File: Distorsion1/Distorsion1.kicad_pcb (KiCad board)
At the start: 2 copper layers, 35 x 79.4 mm, 39 parts, among them J1 Jack-DC, J2 IN, J3 OUT, Sw1 Footswitch, U1 TL082

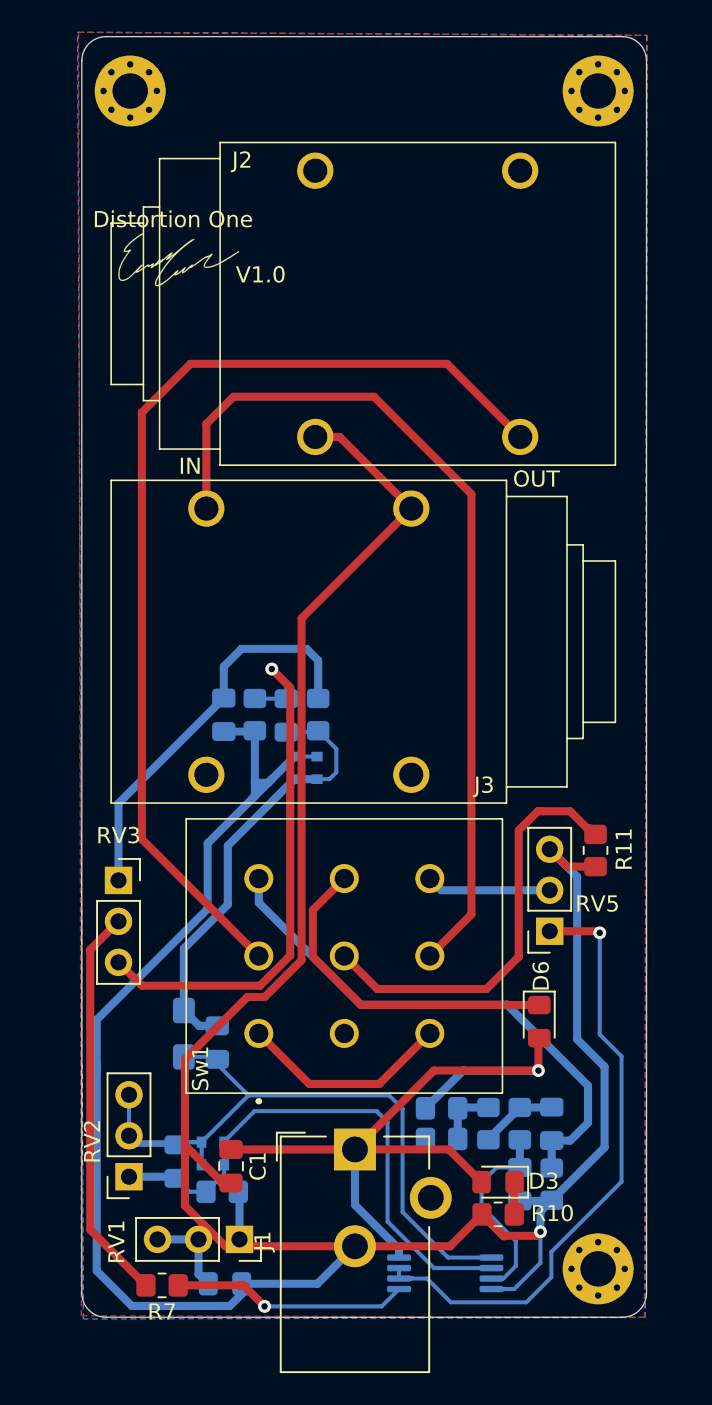
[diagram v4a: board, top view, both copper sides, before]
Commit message: PCB2.0(cambio de parte mecanica y circuito mas cerca de la señal)
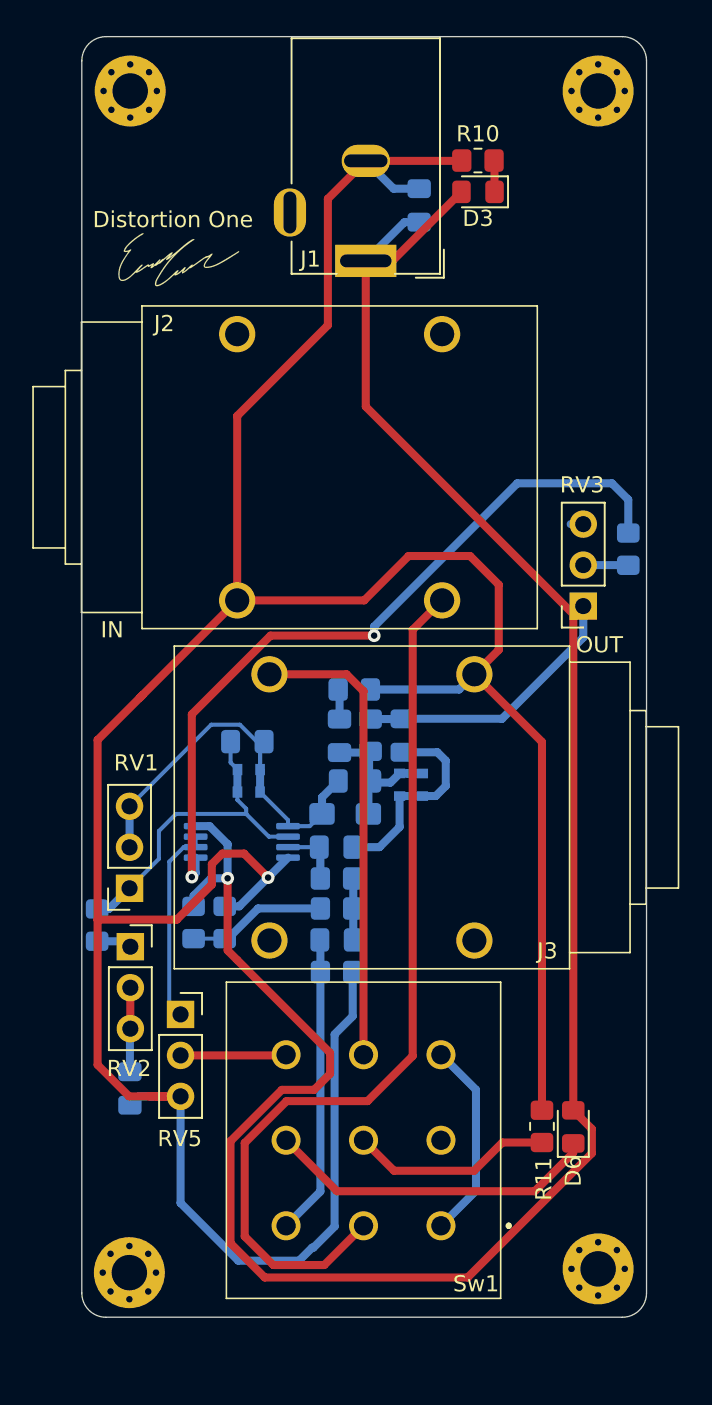
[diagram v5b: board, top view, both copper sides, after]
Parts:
- added REF**: MountingHole_2.2mm_M2_Pad_Via, MountingHole:MountingHole_2.2mm_M2_Pad_Via, F.Cu at (109.9, 128.2)
- C1, R7: moved to B.Cu
- moved R10 65.3 mm to (131.6, 59.3)
- moved D3 61.4 mm to (131.6, 61.2)
- moved C1 60.7 mm to (127.9, 62.1), turned to 90 degrees
- moved J1 55.1 mm to (124.6, 65.5), turned to 180 degrees
- moved R7 54.0 mm to (140.9, 83.4), turned to 270 degrees
- moved RV3 33.4 mm to (138.1, 86.9), turned to 180 degrees
- moved U1 29.6 mm to (116.9, 101.5)
- moved C5 26.4 mm to (117.3, 95.3), turned to 0 degrees
- moved D1 24.6 mm to (117.4, 97.1), turned to 180 degrees
- moved C3 23.8 mm to (122.8, 101.9), turned to 180 degrees
- moved RV5 23.5 mm to (113.1, 112.2), turned to 0 degrees
- moved D2 21.8 mm to (117.3, 98.4), turned to 0 degrees
- moved RV1 19.4 mm to (110.0, 108.0), turned to 0 degrees
- moved R8 19.2 mm to (113.9, 106.5), turned to 270 degrees
- moved R9 19.0 mm to (115.9, 106.5), turned to 90 degrees
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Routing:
- net +12V: track 47.5 -> 136.3 mm
- net Net-(R7-Pad1): track 15.0 -> 47.2 mm, vias 1 -> 2
- net Net-(C8-Pad2): track 34.4 -> 2.65 mm, vias 1 -> 0
- net Net-(RV5-Pad1): track 39.0 -> 12.4 mm, vias 1 -> 0
- net Net-(J3-Pad1): track 54.6 -> 28.8 mm
- net Net-(R7-Pad2): track 24.7 -> 2.79 mm
- net GND: track 192.0 -> 213.7 mm
- net Net-(C5-Pad2): track 45.7 -> 27.1 mm
- net Net-(C6-Pad1): track 27.6 -> 11.0 mm
- net Net-(C2-Pad2): track 33.3 -> 18.6 mm
- net Net-(R11-Pad2): track 26.2 -> 12.6 mm
- net Net-(C5-Pad1): track 33.7 -> 20.8 mm
- net Net-(C3-Pad2): track 12.4 -> 3.91 mm
- net Net-(C9-Pad2): track 24.9 -> 17.2 mm
- net Net-(J2-Pad1): track 63.3 -> 56.5 mm
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- removed copper zone on F.Cu, net (none)
- removed copper zone on B.Cu, net GND
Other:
- board text removed: "V1.0"

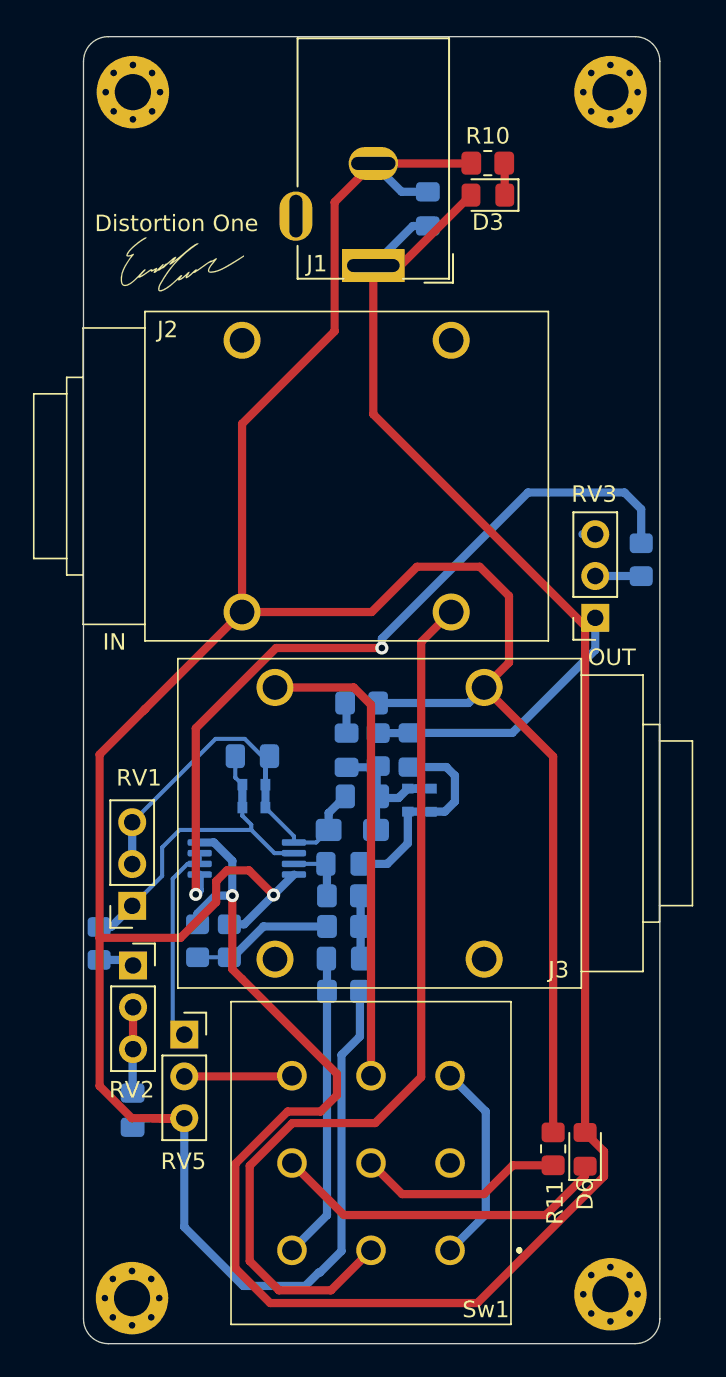
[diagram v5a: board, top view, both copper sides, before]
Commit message: PCB 2.0.1 (añadido de tierra)
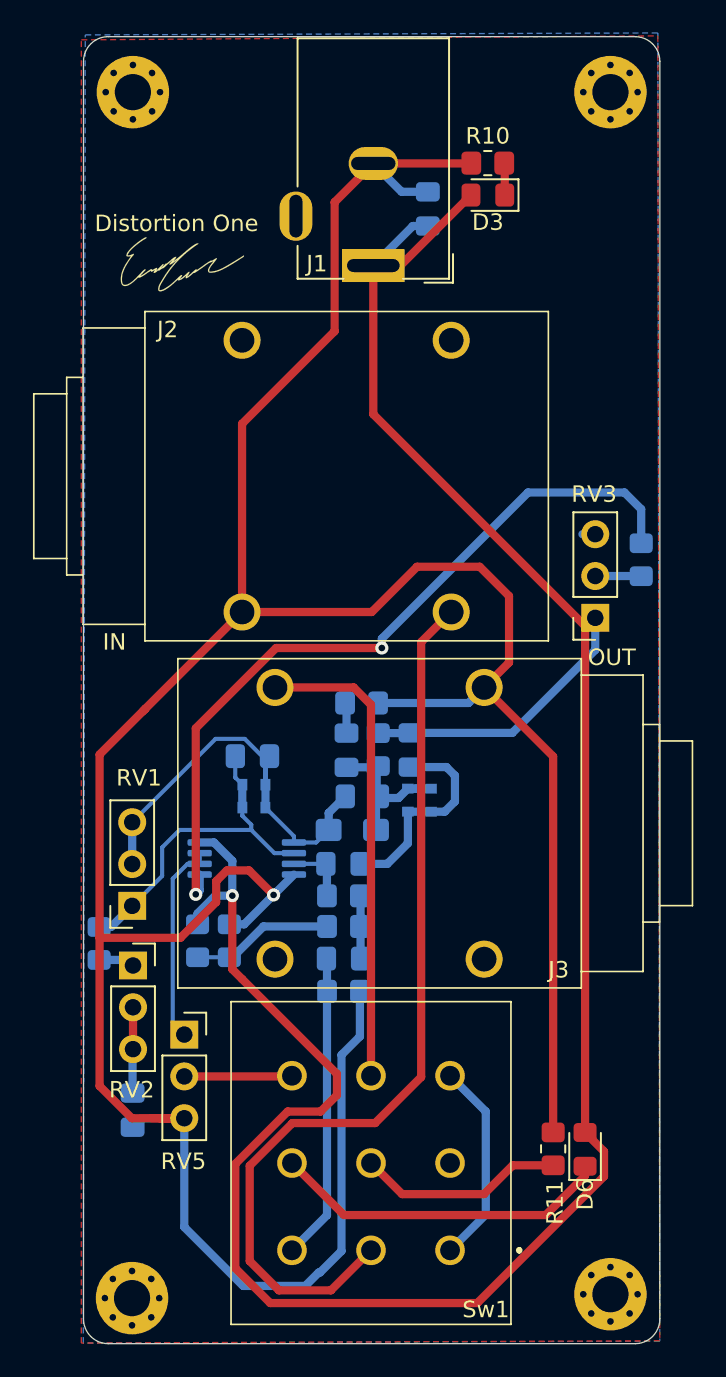
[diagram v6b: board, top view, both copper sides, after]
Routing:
- added copper zone on B.Cu, net GND
- added copper zone on F.Cu, net GND

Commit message: update traces
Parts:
- moved R7 29.9 mm to (112.2, 92.1), turned to 180 degrees
- moved RV3 29.6 mm to (108.8, 91.1), turned to 0 degrees
- moved C9 16.5 mm to (112.2, 87.4), turned to 180 degrees
- moved R5 13.9 mm to (112.2, 89.3), turned to 0 degrees
- moved R6 12.5 mm to (112.2, 96.8)
- moved C8 10.7 mm to (112.3, 94.8), turned to 180 degrees
- moved C5 7.58 mm to (111.5, 100.3), turned to 90 degrees
- moved RV5 7.58 mm to (108.8, 118.4)
- moved C4 5.23 mm to (112.7, 112.4)
- moved C6 4.34 mm to (119.9, 97.1), turned to 270 degrees
- moved R4 4.08 mm to (112.0, 106.5)
- moved D5 2.95 mm to (125.2, 97.3)
- moved D4 2.95 mm to (123.8, 97.3)
- moved C7 1.92 mm to (122.0, 97.6), turned to 270 degrees
- moved D1 1.75 mm to (115.8, 97.9), turned to 270 degrees
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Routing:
- net GND: track 213.7 -> 31.0 mm, vias 1 -> 8
- net Net-(R7-Pad1): track 47.2 -> 15.5 mm
- net +12V: track 136.3 -> 153.9 mm
- net Net-(RV5-Pad1): track 12.4 -> 24.3 mm, vias 0 -> 1
- net Net-(C9-Pad2): track 17.2 -> 5.82 mm
- net Net-(C6-Pad1): track 11.0 -> 22.4 mm
- net Net-(RV5-Pad2): track 6.56 -> 16.3 mm
- net Net-(C4-Pad2): track 5.22 -> 9.55 mm
- net Net-(J2-Pad1): track 56.5 -> 60.5 mm
- net /bypass: track 12.4 -> 15.1 mm
- net Net-(C5-Pad2): track 27.1 -> 24.5 mm
- net Net-(D6-Pad1): track 20.7 -> 22.9 mm
- net Net-(C8-Pad2): track 2.65 -> 4.68 mm
- net Net-(R4-Pad2): track 2.20 -> 3.65 mm
- net Net-(R11-Pad2): track 12.6 -> 13.8 mm
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
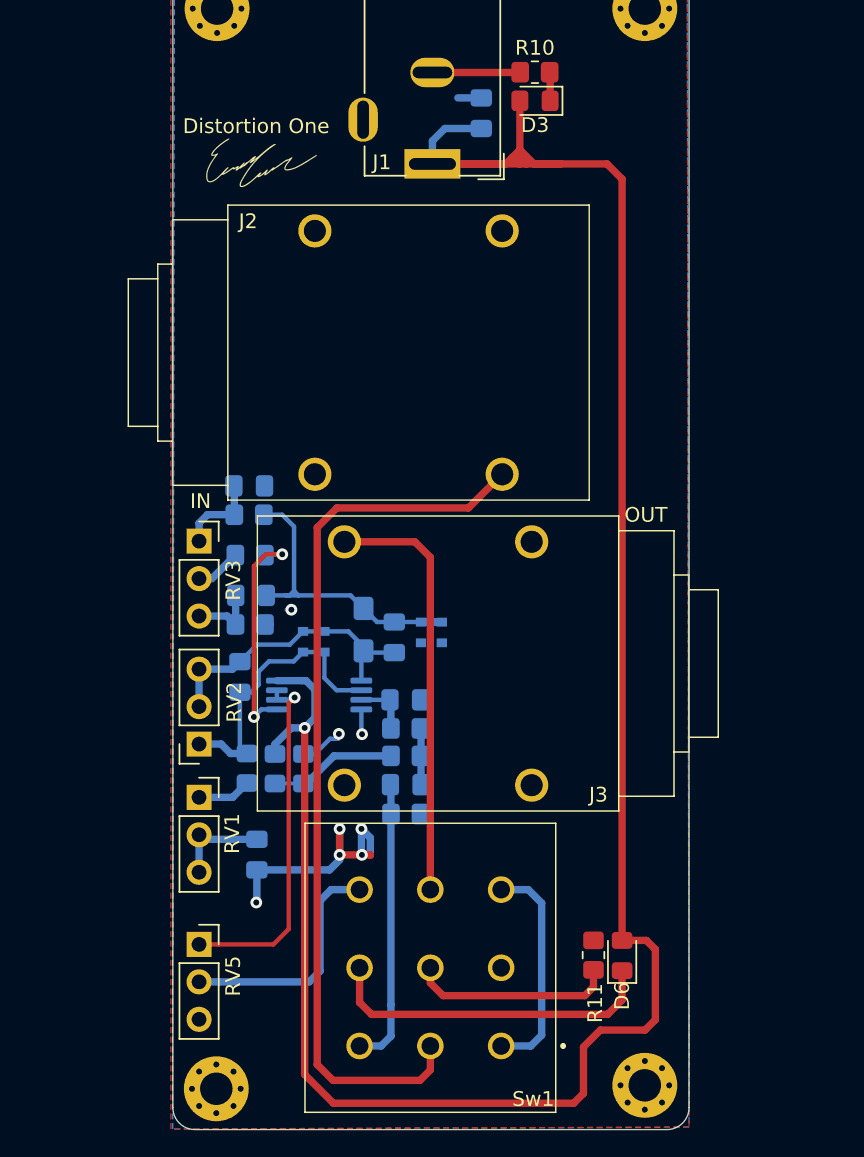
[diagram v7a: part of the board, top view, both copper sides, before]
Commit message: jacks cacados 1 cm
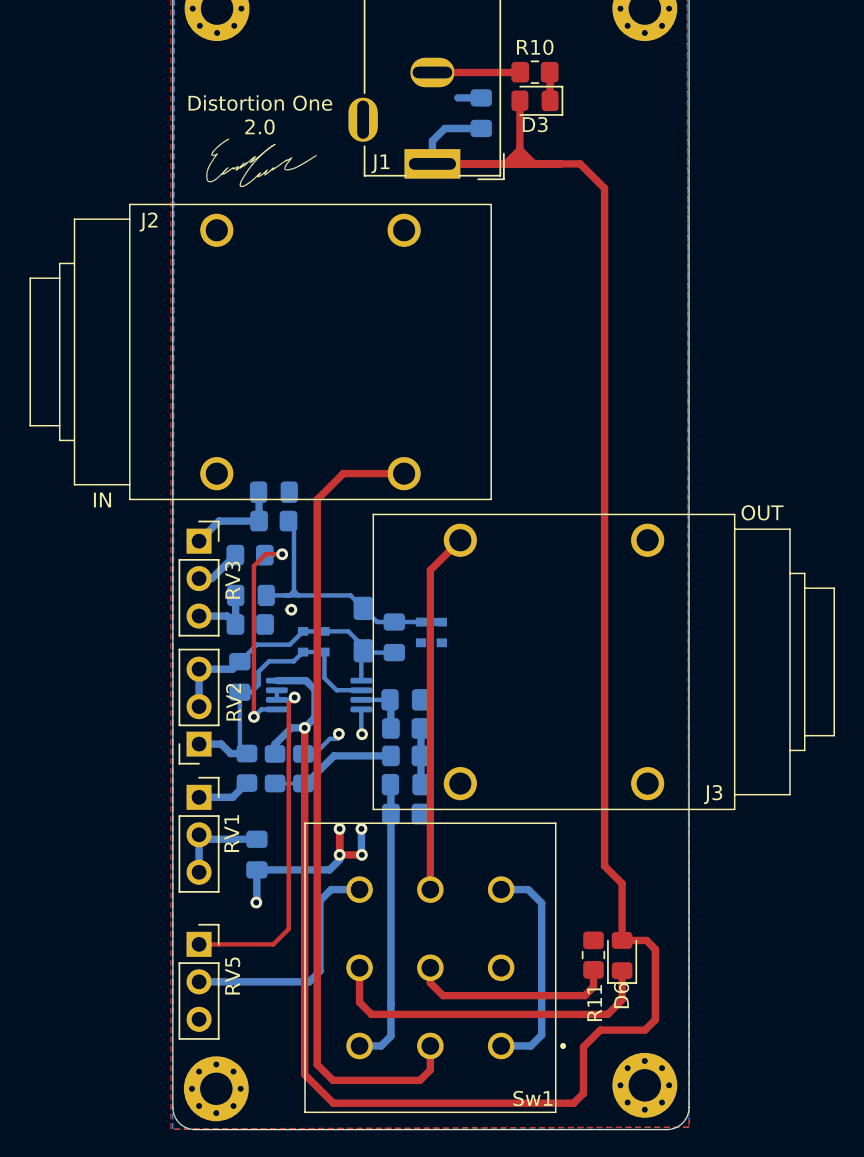
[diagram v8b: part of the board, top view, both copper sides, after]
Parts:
- moved J3 7.86 mm to (126.5, 107.5)
- moved J2 6.65 mm to (122.7, 70.0)
- moved C9 1.73 mm to (113.9, 87.8)
- moved R5 1.73 mm to (113.8, 89.7)
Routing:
- net +12V: track 153.9 -> 161.5 mm
- net Net-(J2-Pad1): track 60.5 -> 55.0 mm
- net Net-(J3-Pad1): track 28.8 -> 24.5 mm
- net GND: track 31.0 -> 28.4 mm
- net Net-(C6-Pad1): track 22.4 -> 20.0 mm
- net Net-(C9-Pad2): track 5.82 -> 6.56 mm
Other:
- board text added: "Distortion One 2.0"
- board text removed: "Distortion One"
